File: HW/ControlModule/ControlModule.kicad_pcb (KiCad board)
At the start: 2 copper layers, 243.8 x 95.2 mm, 98 parts, among them U1 AD8629, U2 STM32L476VETx, U3 LM4132AMF-3.3, U4 TLV70233DBVR

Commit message: updates
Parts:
- added R14: 220R, Resistor_SMD:R_0805_2012Metric_Pad1.15x1.40mm_HandSolder, B.Cu at (293.1, 63.8)
- added R15: 10K, Resistor_SMD:R_0805_2012Metric_Pad1.15x1.40mm_HandSolder, B.Cu at (202.7, 100.3)
- added U_BTNRST1: Tactile_Switch_SPST-NO, 12x12x7_3mmTactilePushButtonMomentary:12x12x7_3mmTactilePushButtonMomentary, F.Cu at (122.7, 64.0)
- C1, C2: value 1u -> 100nF
- C24, C25: value 20pF -> 0pF
- C26, C3, C4: value 1u -> 0F
- C27: value 1u -> oF
- R1, R2, R8, R9: value 10K -> 0R
- R3, R4: value 10K -> 100R
- R6, R7: value 4K7 -> 0R
- U2: value STM32L476VETx -> STM32L496VGTx
- moved TP24 7.41 mm to (184.2, 100.3)
- moved JP6 0.61 mm to (170.1, 127.0)
- moved JP5 0.59 mm to (173.4, 127.0)
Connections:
- JOLED1 pad 5: /Control/NRST -> /Control/OLED_RST
- U2 pad 12: (no net) -> /Control/OLED_RST
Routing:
- net /Control/OLED_RST: track 0.00 -> 26.6 mm
- net +3V3: track 288.1 -> 299.6 mm
- net /Control/NRST: track 57.9 -> 66.0 mm

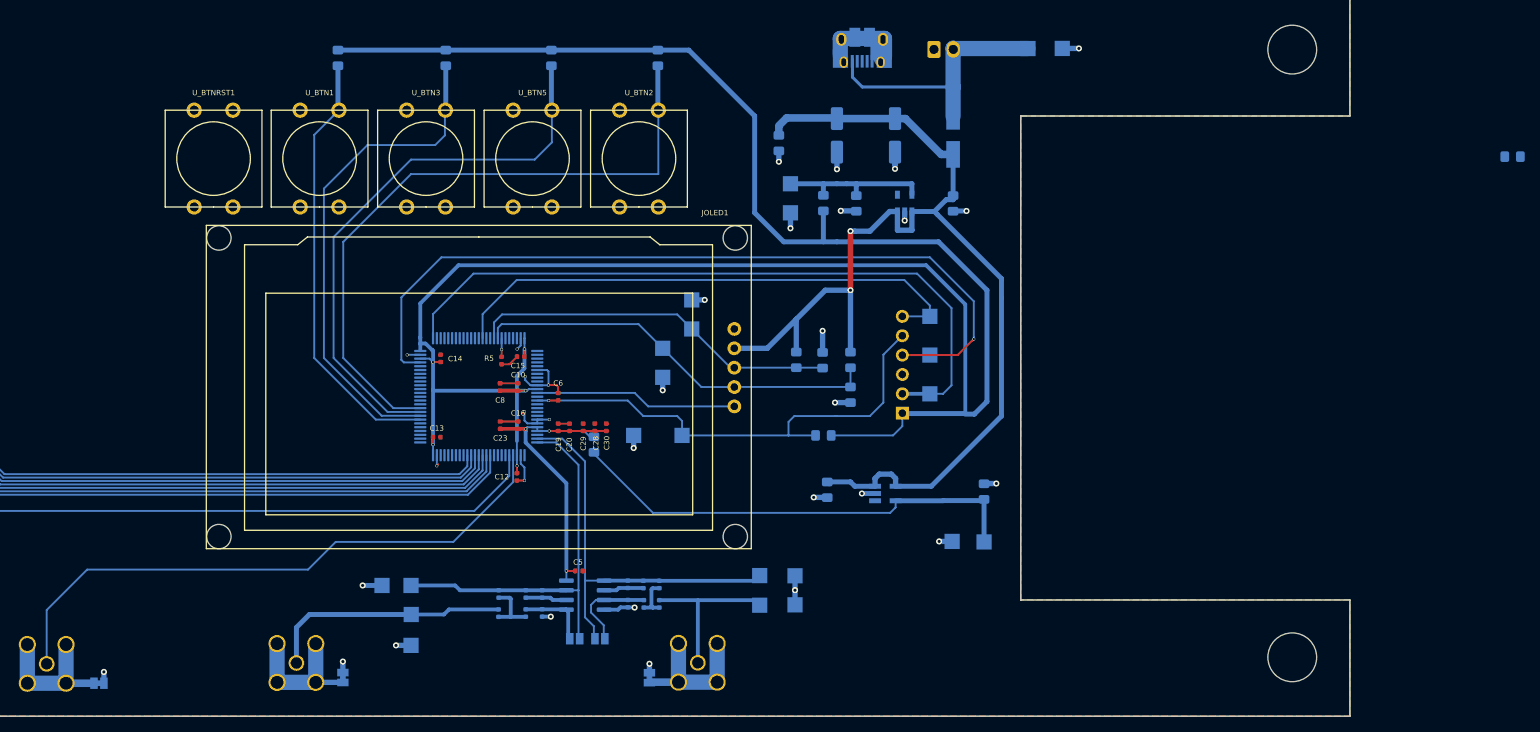
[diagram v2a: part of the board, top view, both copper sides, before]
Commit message: updated HW
- Added front panel NRST switch
- Changed 0402 to 0805 input filter, added NC jumper
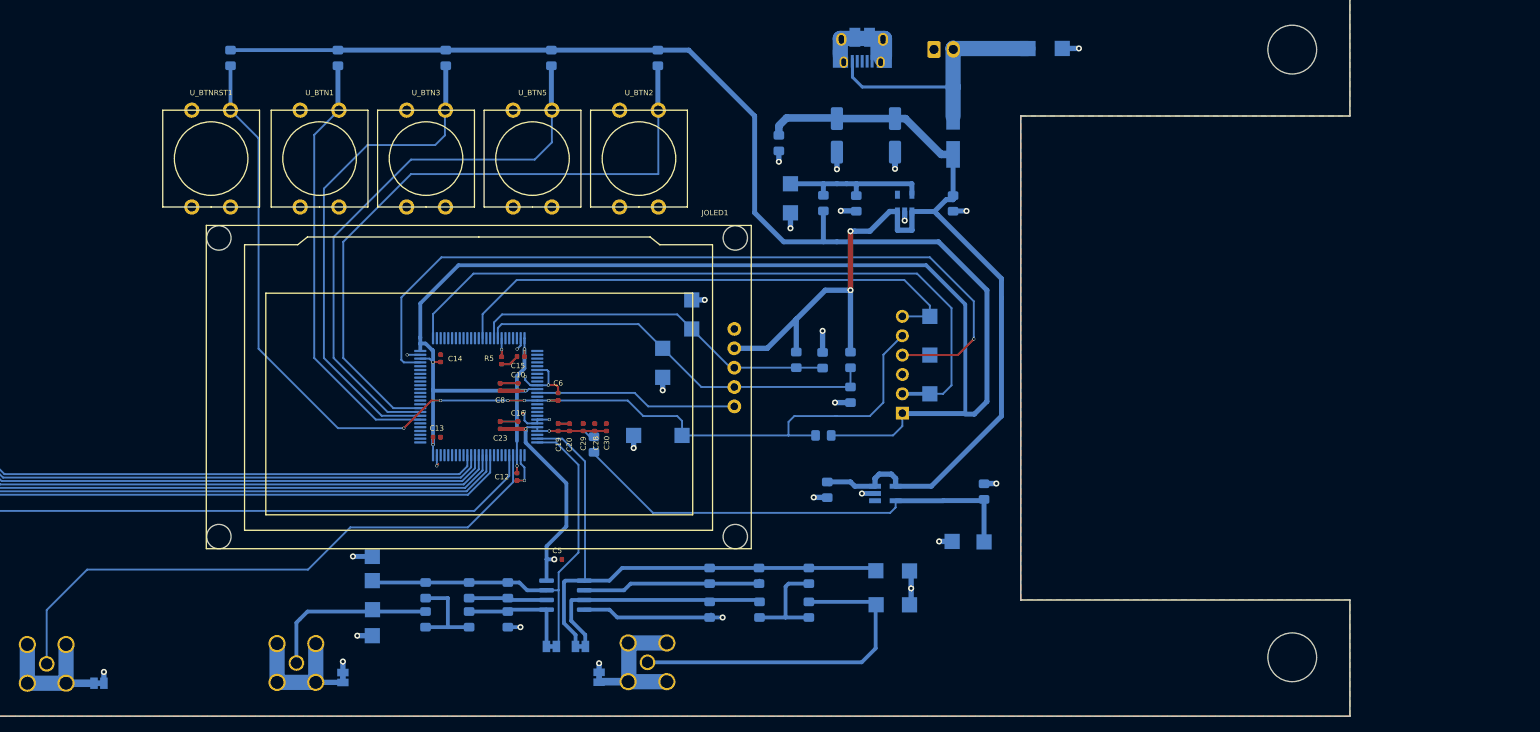
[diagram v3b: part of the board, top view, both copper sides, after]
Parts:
- C1, C2, C26, C27, C3, C4: footprint Capacitor_SMD:C_0402_1005Metric -> Capacitor_SMD:C_0805_2012Metric_Pad1.15x1.40mm_HandSolder
- JP5, JP6: footprint Jumper:SolderJumper-2_P1.3mm_Open_Pad1.0x1.5mm -> Jumper:SolderJumper-2_P1.3mm_Bridged_Pad1.0x1.5mm
- R1, R2, R3, R4, R8, R9: footprint Resistor_SMD:R_0402_1005Metric -> Resistor_SMD:R_0805_2012Metric_Pad1.15x1.40mm_HandSolder
- moved R14 168.7 mm to (124.9, 50.8), turned to 270 degrees
- moved C3 19.7 mm to (200.8, 118.7)
- moved R2 19.6 mm to (200.8, 123.2)
- moved TP2 15.3 mm to (209.6, 122.5)
- moved TP10 15.3 mm to (209.6, 118.1)
- moved C26 15.2 mm to (194.2, 118.7)
- moved R3 15.2 mm to (194.3, 123.2)
- moved TPG10 15.0 mm to (214.0, 118.1)
- moved TPG9 15.0 mm to (214.0, 122.6)
- moved R8 10.8 mm to (187.8, 118.7)
- moved C1 10.8 mm to (187.8, 123.2)
- moved R1 9.61 mm to (150.5, 124.5)
- moved C4 9.60 mm to (150.5, 120.7)
- moved R4 7.48 mm to (156.2, 124.5)
- moved R9 7.46 mm to (156.2, 120.7)
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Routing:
- net /Control/NRST: track 66.0 -> 147.0 mm, vias 1 -> 5
- net /Control/ADCSIG1: track 21.7 -> 46.3 mm
- net /Control/ADCS1: track 53.6 -> 74.3 mm
- net Net-(C1-Pad1): track 11.8 -> 31.8 mm
- net Net-(C26-Pad1): track 5.28 -> 23.5 mm
- net GNDS: track 100.8 -> 116.1 mm
- net +3V3: track 299.6 -> 313.7 mm
- net /Control/ADCSIG2: track 32.2 -> 23.2 mm
- net Net-(C3-Pad1): track 5.59 -> 13.8 mm
- net Net-(C2-Pad2): track 8.75 -> 15.1 mm
- net Net-(C27-Pad1): track 5.46 -> 10.6 mm
- net /Control/ADCS2: track 51.7 -> 56.6 mm
- net Net-(C4-Pad2): track 7.61 -> 12.4 mm
- net +3.3VA: track 44.2 -> 45.4 mm
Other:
- board text added: "CUT JP5/JP6 TO USE OPAMP"
